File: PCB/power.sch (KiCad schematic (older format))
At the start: 35 parts, among them J1 4DB-P108-06, J2 039531-1002, U1 TPS54308, U2 AP2112K-3.3TRG1

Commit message: Fix PU on FAN RPM, Endstops and Grounding
 * Fixes too weak PU on RPM for fans
 * Simplified endstop setup
 * Grounding fixes:
   * GND below SPI bus
   * 3V3 LDO directly attached
     to main PWR source

Fixes #20
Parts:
- R3: value 4.7k -> 1k
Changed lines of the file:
@@
 P 3550 2900
 F 0 "R3" H 3620 2946 50  0000 L CNN
-F 1 "4.7k" H 3620 2855 50  0000 L CNN
+F 1 "1k" H 3620 2855 50  0000 L CNN
 F 2 "Resistor_SMD:R_0603_1608Metric" V 3480 2900 50  0001 C CNN
 F 3 "~" H 3550 2900 50  0001 C CNN

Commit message: Add a P MOSFET to protect the TPS54308
Since I fried two TPS54308 already, I think it would
be best to implement a reverse voltage protection
before the TPS that provides the 5V rail.

To reuse parts, I also switches the battery protection
P MOSFET to the same part.
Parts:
- added D1: MMSZ5240BS-7-F, Diode_SMD:D_SOD-323, symbol Device:D_Zener
- added Q1: PMV50EPEA, Package_TO_SOT_SMD:SOT-23, symbol Device:Q_PMOS_GSD
- added R2: 100k, Resistor_SMD:R_0603_1608Metric, symbol Device:R
- renumbered D1 to D2, D2 to D3, D3 to D4, D4 to D5, R2 to R3, R3 to R4
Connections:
- wire segments 72 -> 78
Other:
- note removed: "TODO: Insert a 100nF?"
- moved on the sheet: C1, C2, C3, C4, C5, C6, L1, R1, R3, U1

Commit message: Add compability for TPS54302
Since the TPS54308 is often not available, we added the
option to also use the TPS54038. This commit added a lot
of components and changed the CSV.
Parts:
- removed D1: MMSZ5240BS-7-F, Diode_SMD:D_SOD-323, symbol Device:D_Zener
- removed Q1: PMV50EPEA, Package_TO_SOT_SMD:SOT-23, symbol Device:Q_PMOS_GSD
- added C7: 75pF, Capacitor_SMD:C_0603_1608Metric, symbol Device:C
- added R1: 511k, Resistor_SMD:R_0603_1608Metric, symbol Device:R
- added R3: 105k, Resistor_SMD:R_0603_1608Metric, symbol Device:R
- added R4: 2k, Resistor_SMD:R_0603_1608Metric, symbol Device:R
- R2: value 100k -> 49.9
- R6: renamed from R3; value 13,7k -> 13.3k
- renumbered C9 to C10, C10 to C11, C11 to C12, C12 to C13, C13 to C14, C14 to C15, C7 to C8, C8 to C9, D2 to D1, D3 to D2, D4 to D3, D5 to D4, R1 to R5, R4 to R7
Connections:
- wire segments 78 -> 75
- no-connect marks 2 -> 5
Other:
- moved on the sheet: C1, C2, C3, C4, C5, C6, L1, R5, R6, U1

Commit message: Plain GND plane, new Debug Header, KILL PIN now RESET
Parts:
- removed TP1: VDD5V, TestPoint:TestPoint_Pad_D1.0mm, symbol Connector:Test_Point
- removed TP2: VDD3V3, TestPoint:TestPoint_Pad_D1.0mm, symbol Connector:Test_Point
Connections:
- wire segments 75 -> 74
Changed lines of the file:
@@
 Wire Wire Line
 	1450 4850 1450 5650
-$Comp
-L Connector:Test_Point TP1
-U 1 1 5B12B288
-P 8500 1150
-F 0 "TP1" H 8600 1300 50  0000 L CNN
-F 1 "VDD5V" H 8600 1200 50  0000 L CNN
-F 2 "TestPoint:TestPoint_Pad_D1.0mm" H 8700 1150 50  0001 C CNN
-F 3 "~" H 8700 1150 50  0001 C CNN
-	1    8500 1150
-	1    0    0    -1
-$EndComp
 Wire Wire Line
 	8950 1150 8500 1150
-Wire Wire Line
-	3850 2750 3550 2750
-$Comp
-L Connector:Test_Point TP2
-U 1 1 5B12E486
-P 3850 2750
-F 0 "TP2" H 3950 2900 50  0000 L CNN
-F 1 "VDD3V3" H 3950 2800 50  0000 L CNN
-F 2 "TestPoint:TestPoint_Pad_D1.0mm" H 4050 2750 50  0001 C CNN
-F 3 "~" H 4050 2750 50  0001 C CNN
-	1    3850 2750
-	1    0    0    -1
-$EndComp
-Wire Wire Line
-	4500 2750 3850 2750
-Connection ~ 3850 2750
 $Comp
 L Device:Fuse F1
@@
 Wire Notes Line
 	9350 650  9350 2250
+Wire Wire Line
+	3550 2750 4500 2750
 $EndSCHEMATC

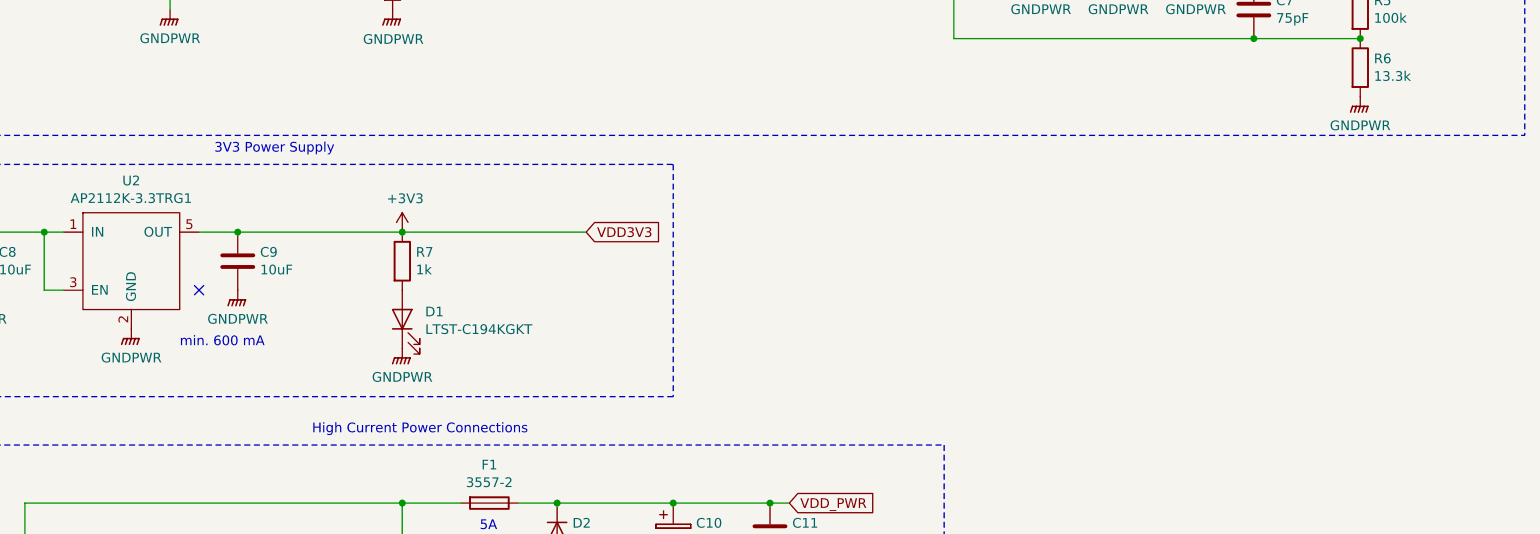
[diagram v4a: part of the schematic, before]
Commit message: Add micro SD card reader and finished GND stitching
Just to be safe, the SD card reader got it's own LDO.
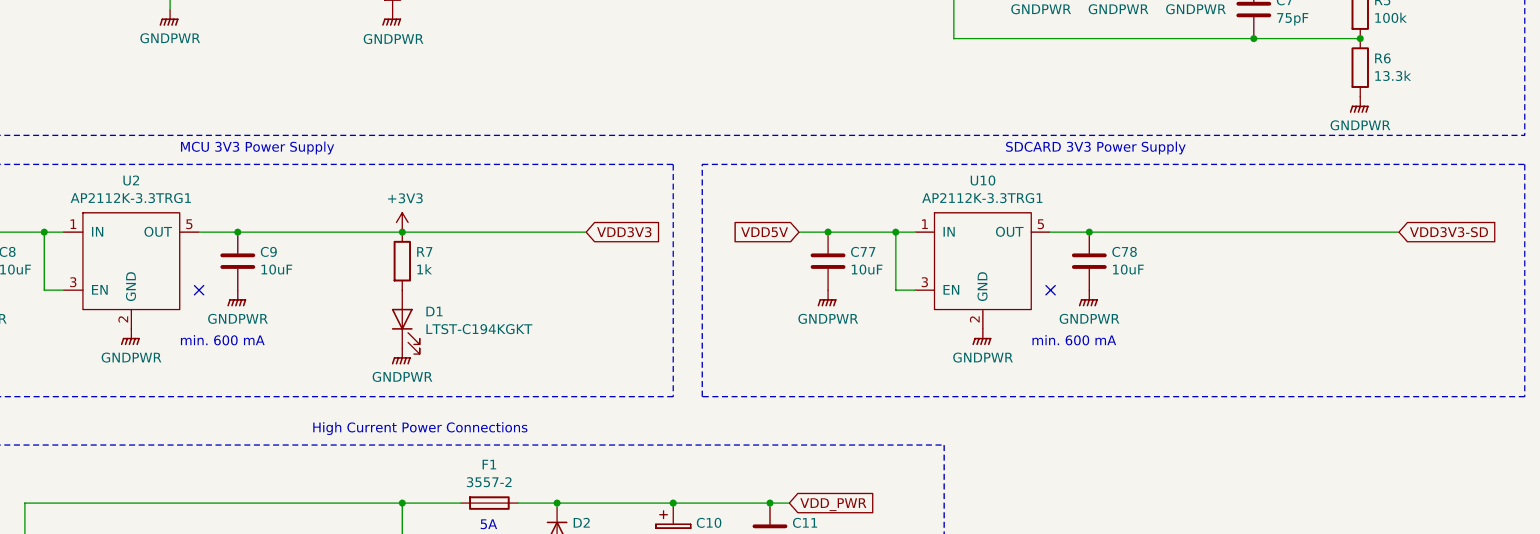
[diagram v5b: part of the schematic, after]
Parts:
- added C77, C78: 10uF, Capacitor_SMD:C_0603_1608Metric, symbol Device:C
- added U10: AP2112K-3.3TRG1, Package_TO_SOT_SMD:SOT-23-5, symbol remram-custom:AP2112K-3.3TRG1
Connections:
- net labels added: VDD3V3-SD
- wire segments 74 -> 81
- no-connect marks 5 -> 6
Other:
- note added: "MCU 3V3 Power Supply"
- note added: "SDCARD 3V3 Power Supply"
- note removed: "3V3 Power Supply"
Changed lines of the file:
@@
 $Descr A4 11693 8268
 encoding utf-8
-Sheet 2 9
+Sheet 2 10
 Title "Power"
 Date ""
@@
 	700  2400 4950 2400
 Text Notes 3200 2350 2    50   ~ 0
-3V3 Power Supply
+MCU 3V3 Power Supply
 $Comp
 L Mechanical:Mounting_Hole_PAD MK1
@@
 Wire Wire Line
 	3550 2750 4500 2750
+Text GLabel 5600 2750 0    50   Input ~ 0
+VDD5V
+Wire Wire Line
+	5600 2750 5750 2750
+Wire Wire Line
+	6100 2750 6100 3050
+Wire Wire Line
+	6100 3050 6200 3050
+Connection ~ 6100 2750
+Wire Wire Line
+	6100 2750 6200 2750
+$Comp
+L Device:C C77
+U 1 1 5BB8A1E0
+P 5750 2900
+F 0 "C77" H 5865 2946 50  0000 L CNN
+F 1 "10uF" H 5865 2855 50  0000 L CNN
+F 2 "Capacitor_SMD:C_0603_1608Metric" H 5788 2750 50  0001 C CNN
+F 3 "~" H 5750 2900 50  0001 C CNN
+	1    5750 2900
+	1    0    0    -1
+$EndComp
+$Comp
+L Device:C C78
+U 1 1 5BB8A1E7
+P 7100 2900
+F 0 "C78" H 7215 2946 50  0000 L CNN
+F 1 "10uF" H 7215 2855 50  0000 L CNN
+F 2 "Capacitor_SMD:C_0603_1608Metric" H 7138 2750 50  0001 C CNN
+F 3 "~" H 7100 2900 50  0001 C CNN
+	1    7100 2900
+	1    0    0    -1
+$EndComp
+Connection ~ 5750 2750
+Wire Wire Line
+	5750 2750 6100 2750
+Text GLabel 8700 2750 2    50   Input ~ 0
+VDD3V3-SD
+Text Notes 6800 3350 0    50   ~ 0
+min. 600 mA
+$Comp
+L power:GNDPWR #PWR0147
+U 1 1 5BB8A206
+P 7100 3050
+F 0 "#PWR0147" H 7100 2850 50  0001 C CNN
+F 1 "GNDPWR" H 7100 2900 50  0000 C CNN
+F 2 "" H 7100 3000 50  0001 C CNN
+F 3 "" H 7100 3000 50  0001 C CNN
+	1    7100 3050
+	1    0    0    -1
+$EndComp
+$Comp
+L power:GNDPWR #PWR0146
+U 1 1 5BB8A20C
+P 6550 3250
+F 0 "#PWR0146" H 6550 3050 50  0001 C CNN
+F 1 "GNDPWR" H 6550 3100 50  0000 C CNN
+F 2 "" H 6550 3200 50  0001 C CNN
+F 3 "" H 6550 3200 50  0001 C CNN
+	1    6550 3250
+	1    0    0    -1
+$EndComp
+$Comp
+L power:GNDPWR #PWR0145
+U 1 1 5BB8A212
+P 5750 3050
+F 0 "#PWR0145" H 5750 2850 50  0001 C CNN
+F 1 "GNDPWR" H 5750 2900 50  0000 C CNN
+F 2 "" H 5750 3000 50  0001 C CNN
+F 3 "" H 5750 3000 50  0001 C CNN
+	1    5750 3050
+	1    0    0    -1
+$EndComp
+Wire Notes Line
+	9350 2400 9350 3600
+Wire Notes Line
+	9350 3600 5100 3600
+Wire Notes Line
+	5100 3600 5100 2400
+Wire Notes Line
+	5100 2400 9350 2400
+Text Notes 7600 2350 2    50   ~ 0
+SDCARD 3V3 Power Supply
+$Comp
+L remram-custom:AP2112K-3.3TRG1 U10
+U 1 1 5BB8A21D
+P 6550 2850
+F 0 "U10" H 6550 3215 50  0000 C CNN
+F 1 "AP2112K-3.3TRG1" H 6550 3124 50  0000 C CNN
+F 2 "Package_TO_SOT_SMD:SOT-23-5" H 6550 2850 50  0001 C CNN
+F 3 "https://www.mouser.de/datasheet/2/115/AP2112-271550.pdf" H 6550 2850 50  0001 C CNN
+	1    6550 2850
+	1    0    0    -1
+$EndComp
+Wire Wire Line
+	6900 2750 7100 2750
+Connection ~ 7100 2750
+NoConn ~ 6900 3050
+Wire Wire Line
+	7100 2750 8700 2750
 $EndSCHEMATC

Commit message: New item designations and fixes some small manufacturing issues
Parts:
- renumbered C8 to C1, C15 to C10, C1 to C11, C77 to C12, C4 to C13, C78 to C14, C5 to C15, C6 to C16, C7 to C17, C9 to C3, C3 to C4, C10 to C5, C12 to C6, C14 to C7, C11 to C8, C13 to C9, R3 to R2, R7 to R3, R2 to R5, R5 to R6, R6 to R7, U2 to U1, U1 to U2, U10 to U3

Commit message: Fixes of v1.3 errors
 * Fixed missing GND connection for SD card detect
 * Optimized solder mask clearance from 0.2 to 0.05
 * Changed 3.3V LDO
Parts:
- MK1, MK2, MK3, MK4: symbol Mechanical:Mounting_Hole_PAD -> remram-rescue:Mounting_Hole_PAD-Mechanical
- U1, U3: value AP2112K-3.3TRG1 -> AP7365-33WG-7
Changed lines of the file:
@@
 MCU 3V3 Power Supply
 $Comp
-L Mechanical:Mounting_Hole_PAD MK1
+L remram-rescue:Mounting_Hole_PAD-Mechanical MK1
 U 1 1 5B0578B3
 P 2250 7250
@@
 $EndComp
 $Comp
-L Mechanical:Mounting_Hole_PAD MK2
+L remram-rescue:Mounting_Hole_PAD-Mechanical MK2
 U 1 1 5B0578BA
 P 3450 7250
@@
 $EndComp
 $Comp
-L Mechanical:Mounting_Hole_PAD MK3
+L remram-rescue:Mounting_Hole_PAD-Mechanical MK3
 U 1 1 5B0578C1
 P 4500 7250
@@
 $EndComp
 $Comp
-L Mechanical:Mounting_Hole_PAD MK4
+L remram-rescue:Mounting_Hole_PAD-Mechanical MK4
 U 1 1 5B0578C8
 P 5500 7250
@@
 P 2150 2850
 F 0 "U1" H 2150 3215 50  0000 C CNN
-F 1 "AP2112K-3.3TRG1" H 2150 3124 50  0000 C CNN
+F 1 "AP7365-33WG-7" H 2150 3124 50  0000 C CNN
 F 2 "Package_TO_SOT_SMD:SOT-23-5" H 2150 2850 50  0001 C CNN
-F 3 "https://www.mouser.de/datasheet/2/115/AP2112-271550.pdf" H 2150 2850 50  0001 C CNN
+F 3 "https://www.mouser.de/datasheet/2/115/AP7365-86154.pdf" H 2150 2850 50  0001 C CNN
 	1    2150 2850
 	1    0    0    -1
@@
 P 6550 2850
 F 0 "U3" H 6550 3215 50  0000 C CNN
-F 1 "AP2112K-3.3TRG1" H 6550 3124 50  0000 C CNN
+F 1 "AP7365-33WG-7" H 6550 3124 50  0000 C CNN
 F 2 "Package_TO_SOT_SMD:SOT-23-5" H 6550 2850 50  0001 C CNN
-F 3 "https://www.mouser.de/datasheet/2/115/AP2112-271550.pdf" H 6550 2850 50  0001 C CNN
+F 3 "https://www.mouser.de/datasheet/2/115/AP7365-86154.pdf" H 6550 2850 50  0001 C CNN
 	1    6550 2850
 	1    0    0    -1
